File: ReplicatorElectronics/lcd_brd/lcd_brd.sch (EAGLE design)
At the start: 10 parts, among them J1 SBH11-PBPC-D17-ST-BK, J2 101-00708-64, U1 PETERATMEGA644_LCD37

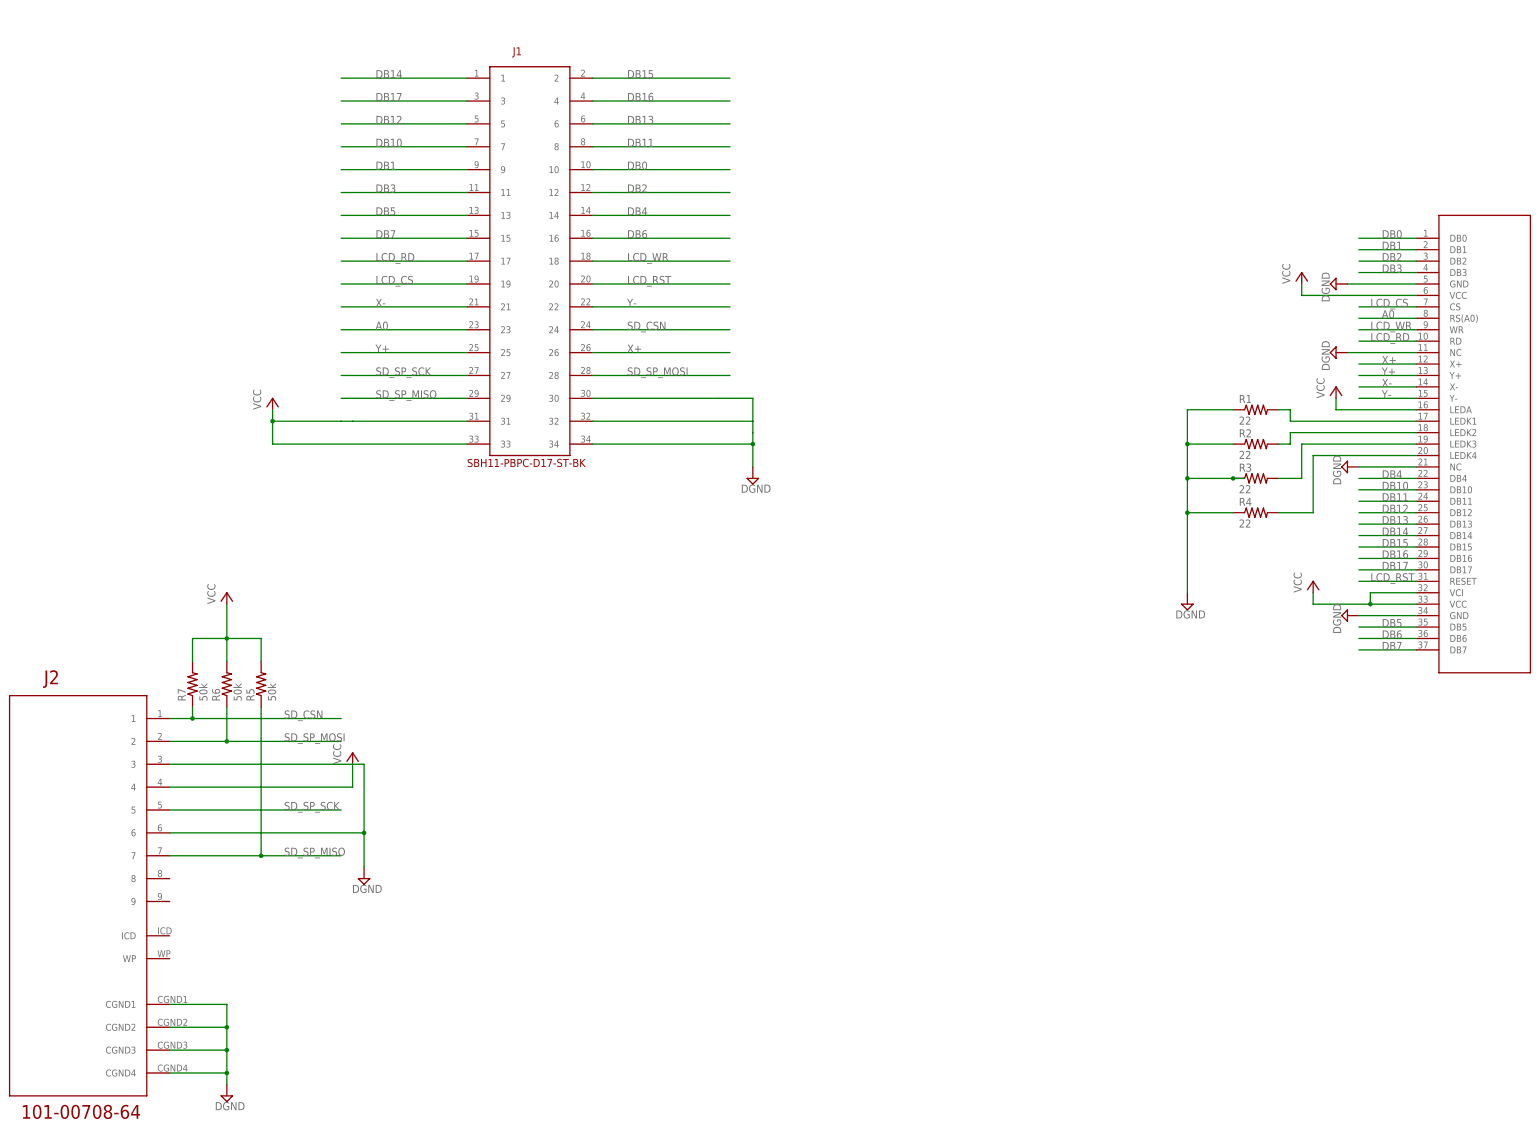
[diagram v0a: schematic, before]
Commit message: 6/19/12: LCD Board layout complete with desired LCD footprint. DXF file updated.
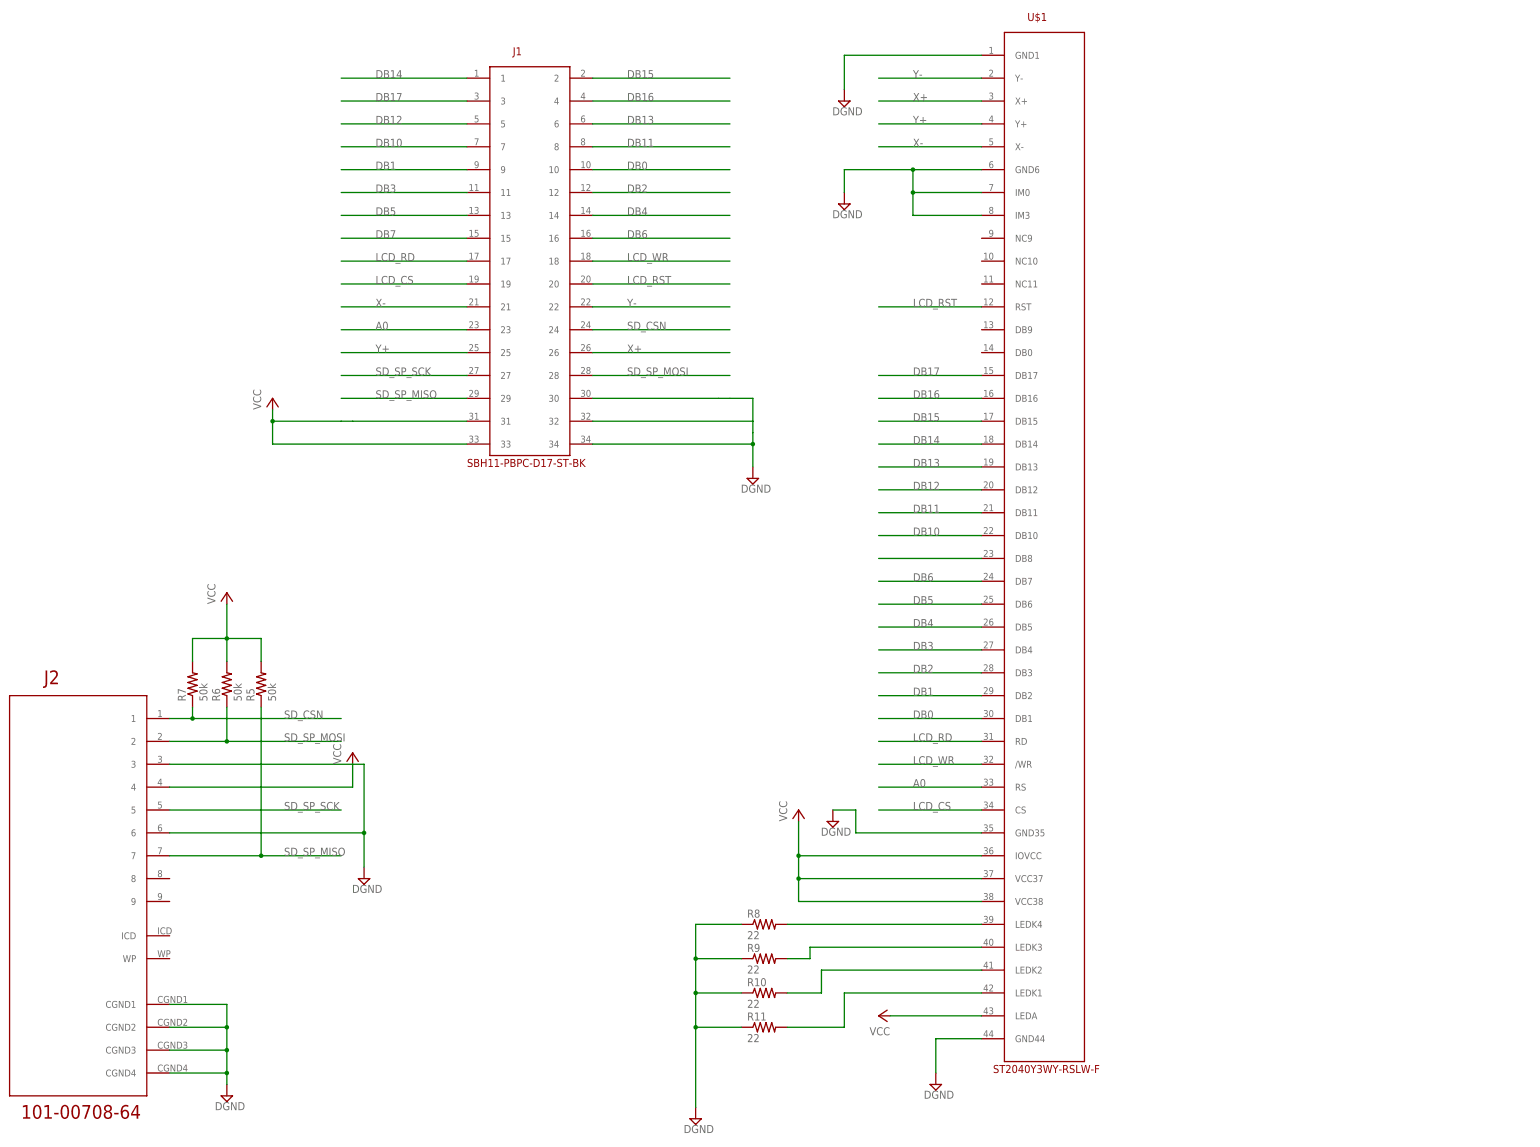
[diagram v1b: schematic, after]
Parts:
- removed R1, R2, R3, R4: 22, resistor:R-US_R0603
- removed U1: PETERATMEGA644_LCD37, microtouch:PETERATMEGA644_LCD37
- added R10, R11, R8, R9: 22, resistor:R-US_R0603
- added U$1: ST2040Y3WY-RSLW-F, ST2040Y3WY-RSLW-F:ST2040Y3WY-RSLW-F
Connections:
- removed net N$1: R1.2, U1.LEDK1
- removed net N$3: R2.2, U1.LEDK2
- removed net N$4: R3.2, U1.LEDK3
- removed net N$6: R4.2, U1.LEDK4
- new net N$12: R8.2, U$1.LEDK4
- new net N$13: R9.2, U$1.LEDK3
- new net N$14: R10.2, U$1.LEDK2
- new net N$15: R11.2, U$1.LEDK1
- net A0: now also U$1.RS; no longer U1.RS(A0)
- net DB0: now also U$1.DB1; no longer U1.DB0
- net DB1: now also U$1.DB2; no longer U1.DB1
- net DB10: now also U$1.DB10; no longer U1.DB10
- net DB11: now also U$1.DB11; no longer U1.DB11
- net DB12: now also U$1.DB12; no longer U1.DB12
- net DB13: now also U$1.DB13; no longer U1.DB13
- net DB14: now also U$1.DB14; no longer U1.DB14
- net DB15: now also U$1.DB15; no longer U1.DB15
- net DB16: now also U$1.DB16; no longer U1.DB16
- net DB17: now also U$1.DB17; no longer U1.DB17
- net DB2: now also U$1.DB3; no longer U1.DB2
- net DB3: now also U$1.DB4; no longer U1.DB3
- net DB4: now also U$1.DB5; no longer U1.DB4
- net DB5: now also U$1.DB6; no longer U1.DB5
- net DB6: now also U$1.DB7; no longer U1.DB6
- net DB7: now also U$1.DB8; no longer U1.DB7
- net DGND: now also R10.1, R11.1, R8.1, R9.1, U$1.GND1, U$1.GND35, U$1.GND44, U$1.GND6, U$1.IM0, U$1.IM3; no longer R1.1, R2.1, R3.1, R4.1, U1.GND@1, U1.GND@2, U1.NC@1, U1.NC@2
- net LCD_CS: now also U$1.CS; no longer U1.CS
- net LCD_RD: now also U$1.RD; no longer U1.RD
- net LCD_RST: now also U$1.RST; no longer U1.RESET
- net LCD_WR: now also U$1./WR; no longer U1.WR
- net VCC: now also U$1.IOVCC, U$1.LEDA, U$1.VCC37, U$1.VCC38; no longer U1.LEDA, U1.VCC@1, U1.VCC@2, U1.VCI
- net X+: now also U$1.X+; no longer U1.X+
- net X-: now also U$1.X-; no longer U1.X-
- net Y+: now also U$1.Y+; no longer U1.Y+
- net Y-: now also U$1.Y-; no longer U1.Y-
